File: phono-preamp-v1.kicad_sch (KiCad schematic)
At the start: 0 parts

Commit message: Complete setup of schematic page
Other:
- title: (none) -> Practical MM amplifier #3
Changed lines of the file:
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@@
 	(generator_version "9.0")
 	(paper "A4")
+	(title_block
+		(title "Practical MM amplifier #3")
+		(date "2025-12-29")
+		(rev "0.1")
+		(comment 1 "Small Signal Audio Design, 4th Edition, by Douglas Self")
+		(comment 2 "Based on Signal Transfer design")
+	)
 	(sheet_instances
 		(path "/"

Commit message: Add symbols to schematic
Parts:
- added C1, C18, C2: C_Polarized, symbol Device:C_Polarized
- added C10, C11, C12, C13, C14, C15, C16, C17, C3, C4, C5, C6, C7, C8, C9: C, symbol Device:C
- added J1, J2: Screw_Terminal_01x02, TerminalBlock_4Ucon:TerminalBlock_4Ucon_1x02_P3.50mm_Horizontal, symbol Connector:Screw_Terminal_01x02
- added R1, R10, R11, R12, R13, R14, R15, R2, R3, R4, R5, R6, R7, R8, R9: R, symbol Device:R
- added U1, U2: NE5534, symbol Amplifier_Operational:NE5534

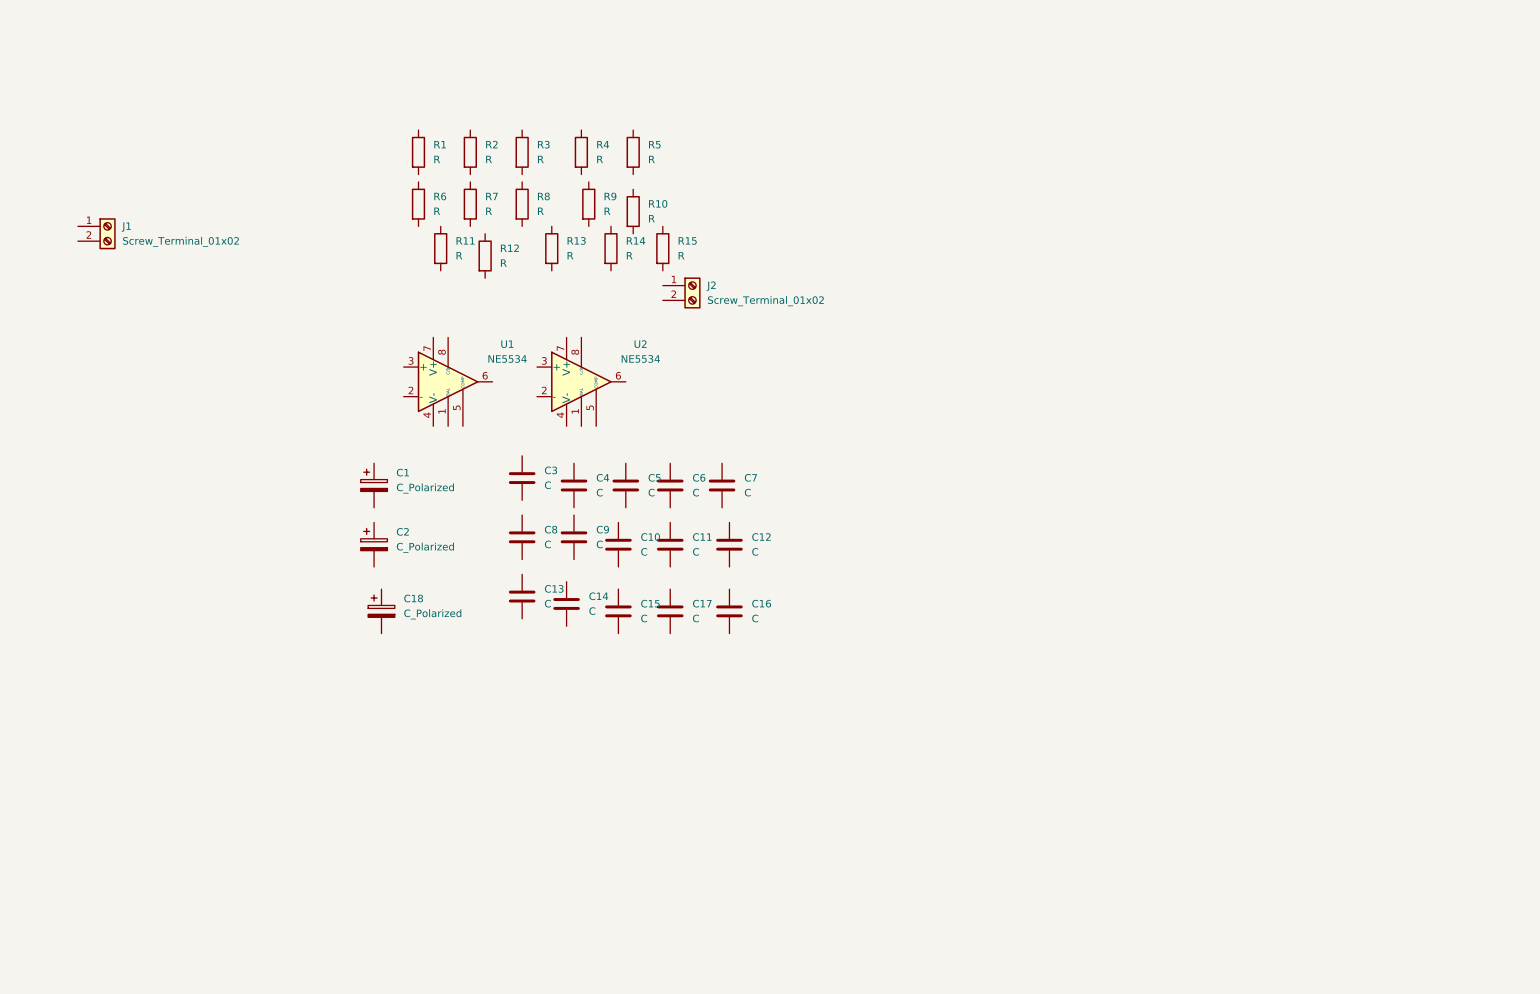
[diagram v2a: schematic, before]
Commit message: Arrange symbols; add footprints
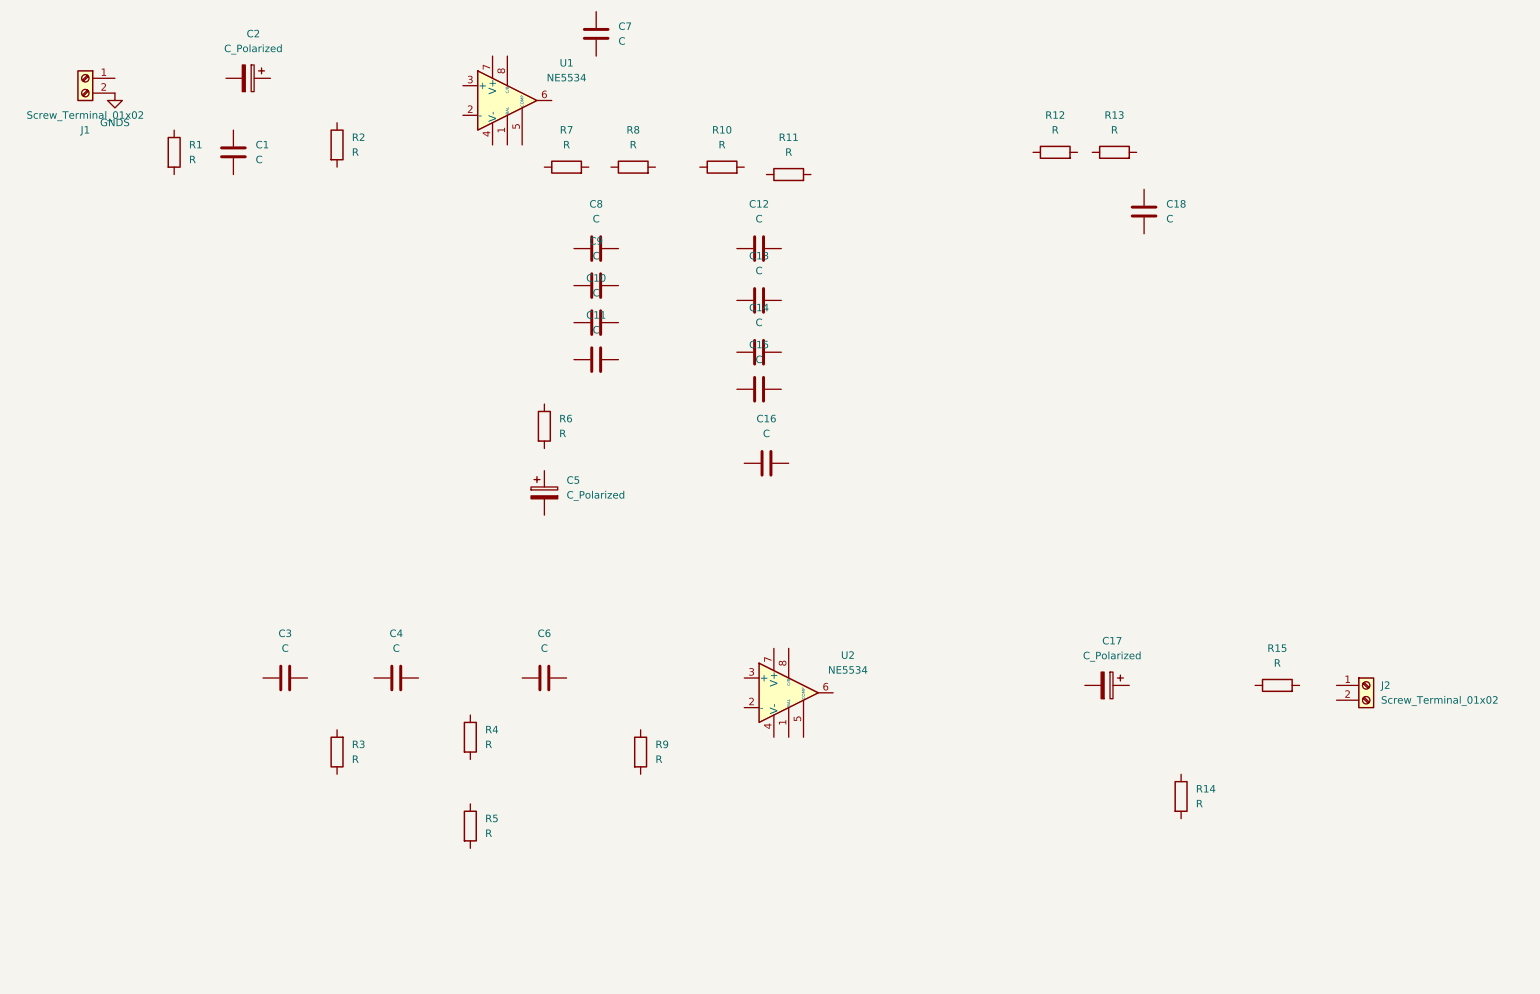
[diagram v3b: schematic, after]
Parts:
- C1: renamed from C3; footprint (none) -> Capacitor_SMD:C_0805_2012Metric_Pad1.18x1.45mm_HandSolder
- C10: renamed from C7; footprint (none) -> Capacitor_SMD:C_0805_2012Metric_Pad1.18x1.45mm_HandSolder
- C11: renamed from C8; footprint (none) -> Capacitor_SMD:C_0805_2012Metric_Pad1.18x1.45mm_HandSolder
- C12: renamed from C13; footprint (none) -> Capacitor_SMD:C_0805_2012Metric_Pad1.18x1.45mm_HandSolder
- C13: renamed from C9; footprint (none) -> Capacitor_SMD:C_0805_2012Metric_Pad1.18x1.45mm_HandSolder
- C14: renamed from C10; footprint (none) -> Capacitor_SMD:C_0805_2012Metric_Pad1.18x1.45mm_HandSolder
- C15: renamed from C11; footprint (none) -> Capacitor_SMD:C_0805_2012Metric_Pad1.18x1.45mm_HandSolder
- C16: renamed from C12; footprint (none) -> Capacitor_SMD:C_0805_2012Metric_Pad1.18x1.45mm_HandSolder
- C17: renamed from C18; footprint (none) -> Capacitor_THT:C_Radial_D4.0mm_H7.0mm_P1.50mm
- C18: renamed from C14; footprint (none) -> Capacitor_SMD:C_0805_2012Metric_Pad1.18x1.45mm_HandSolder
- C2: renamed from C1; footprint (none) -> Capacitor_THT:C_Radial_D6.3mm_H11.0mm_P2.50mm
- C3: renamed from C15; footprint (none) -> Capacitor_SMD:C_0805_2012Metric_Pad1.18x1.45mm_HandSolder
- C4: renamed from C17; footprint (none) -> Capacitor_SMD:C_0805_2012Metric_Pad1.18x1.45mm_HandSolder
- C5: renamed from C2; footprint (none) -> Capacitor_THT:C_Radial_D6.3mm_H11.0mm_P2.50mm
- C6: renamed from C16; footprint (none) -> Capacitor_SMD:C_0805_2012Metric_Pad1.18x1.45mm_HandSolder
- C7: renamed from C4; footprint (none) -> Capacitor_SMD:C_0805_2012Metric_Pad1.18x1.45mm_HandSolder
- C8: renamed from C5; footprint (none) -> Capacitor_SMD:C_0805_2012Metric_Pad1.18x1.45mm_HandSolder
- C9: renamed from C6; footprint (none) -> Capacitor_SMD:C_0805_2012Metric_Pad1.18x1.45mm_HandSolder
- R1, R14, R15, R2: footprint (none) -> Resistor_SMD:R_0805_2012Metric_Pad1.20x1.40mm_HandSolder
- R10: renamed from R6; footprint (none) -> Resistor_SMD:R_0805_2012Metric_Pad1.20x1.40mm_HandSolder
- R11: renamed from R7; footprint (none) -> Resistor_SMD:R_0805_2012Metric_Pad1.20x1.40mm_HandSolder
- R12: renamed from R8; footprint (none) -> Resistor_SMD:R_0805_2012Metric_Pad1.20x1.40mm_HandSolder
- R13: renamed from R9; footprint (none) -> Resistor_SMD:R_0805_2012Metric_Pad1.20x1.40mm_HandSolder
- R3: renamed from R10; footprint (none) -> Resistor_SMD:R_0805_2012Metric_Pad1.20x1.40mm_HandSolder
- R4: renamed from R11; footprint (none) -> Resistor_SMD:R_0805_2012Metric_Pad1.20x1.40mm_HandSolder
- R5: renamed from R12; footprint (none) -> Resistor_SMD:R_0805_2012Metric_Pad1.20x1.40mm_HandSolder
- R6: renamed from R5; footprint (none) -> Resistor_SMD:R_0805_2012Metric_Pad1.20x1.40mm_HandSolder
- R7: renamed from R3; footprint (none) -> Resistor_SMD:R_0805_2012Metric_Pad1.20x1.40mm_HandSolder
- R8: renamed from R4; footprint (none) -> Resistor_SMD:R_0805_2012Metric_Pad1.20x1.40mm_HandSolder
- R9: renamed from R13; footprint (none) -> Resistor_SMD:R_0805_2012Metric_Pad1.20x1.40mm_HandSolder
- U1, U2: footprint (none) -> Package_SO:SOIC-8_3.9x4.9mm_P1.27mm
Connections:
- net GNDS: now reaches J1.2 (Pin_2)
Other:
- moved on the sheet: C1, C10, C11, C12, C13, C14, C15, C16, C17, C18, C2, C3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

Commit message: Add component values
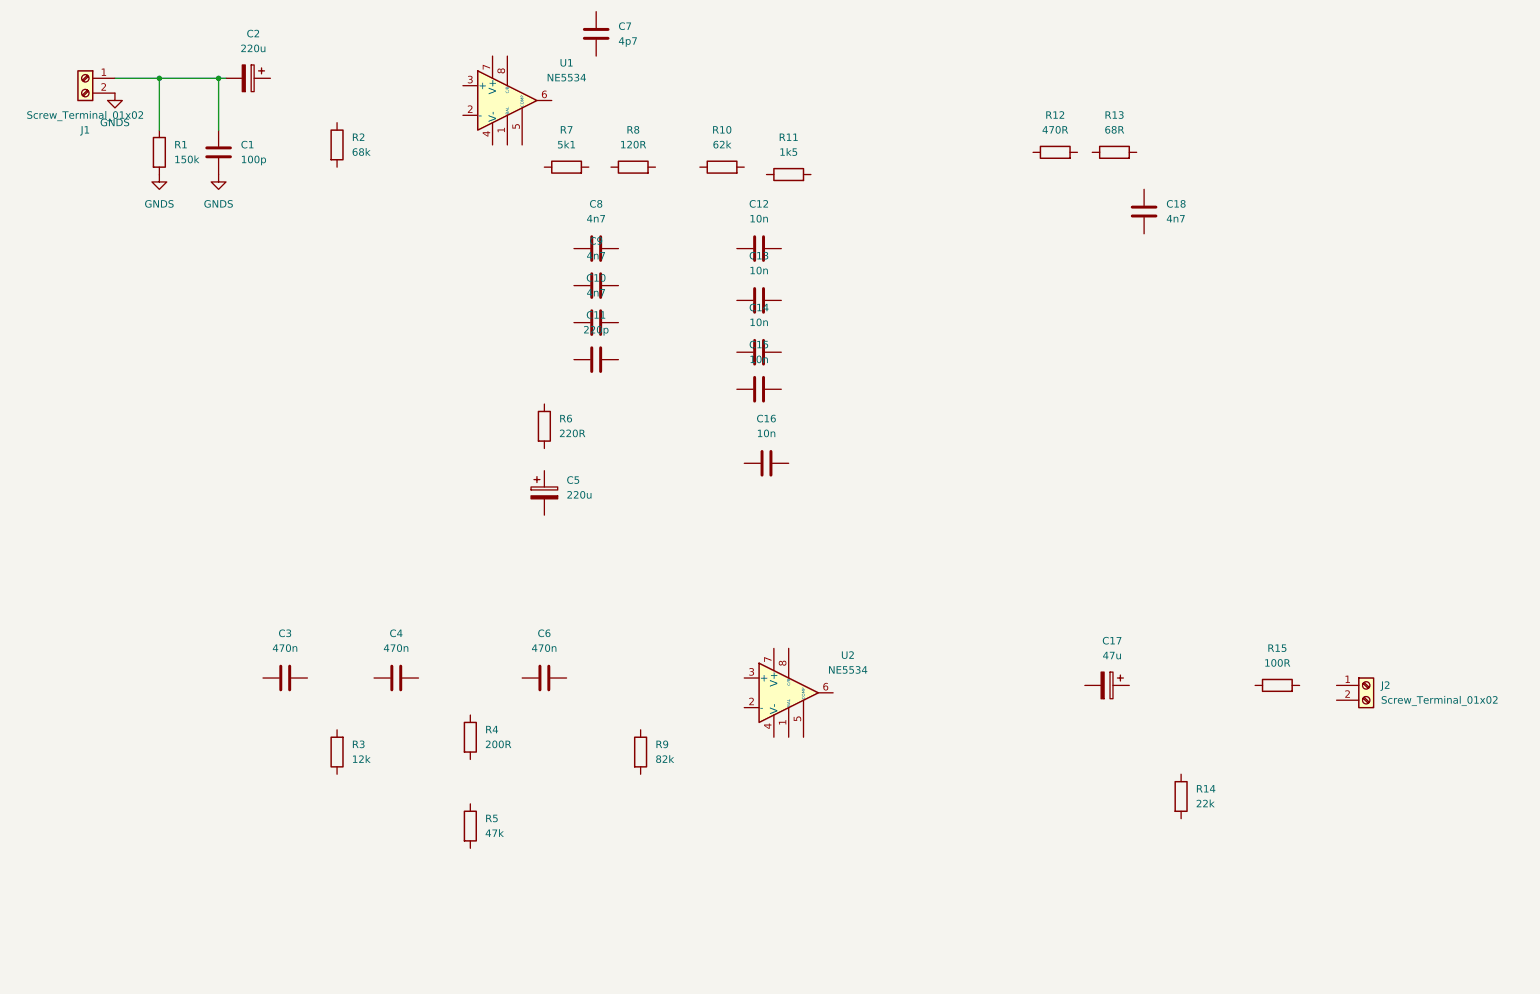
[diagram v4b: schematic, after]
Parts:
- C1: value C -> 100p
- C10, C18, C8, C9: value C -> 4n7
- C11: value C -> 220p
- C12, C13, C14, C15, C16: value C -> 10n
- C17: value C_Polarized -> 47u
- C2, C5: value C_Polarized -> 220u
- C3, C4, C6: value C -> 470n
- C7: value C -> 4p7
- R1: value R -> 150k
- R10: value R -> 62k
- R11: value R -> 1k5
- R12: value R -> 470R
- R13: value R -> 68R
- R14: value R -> 22k
- R15: value R -> 100R
- R2: value R -> 68k
- R3: value R -> 12k
- R4: value R -> 200R
- R5: value R -> 47k
- R6: value R -> 220R
- R7: value R -> 5k1
- R8: value R -> 120R
- R9: value R -> 82k
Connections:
- net GNDS: now also C1.2, R1.2
- net at C2.2: now also C1.1, J1.1 (Pin_1), R1.1
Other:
- moved on the sheet: C1, R1

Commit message: Reannotate symbols; clean up schematic; run simulations
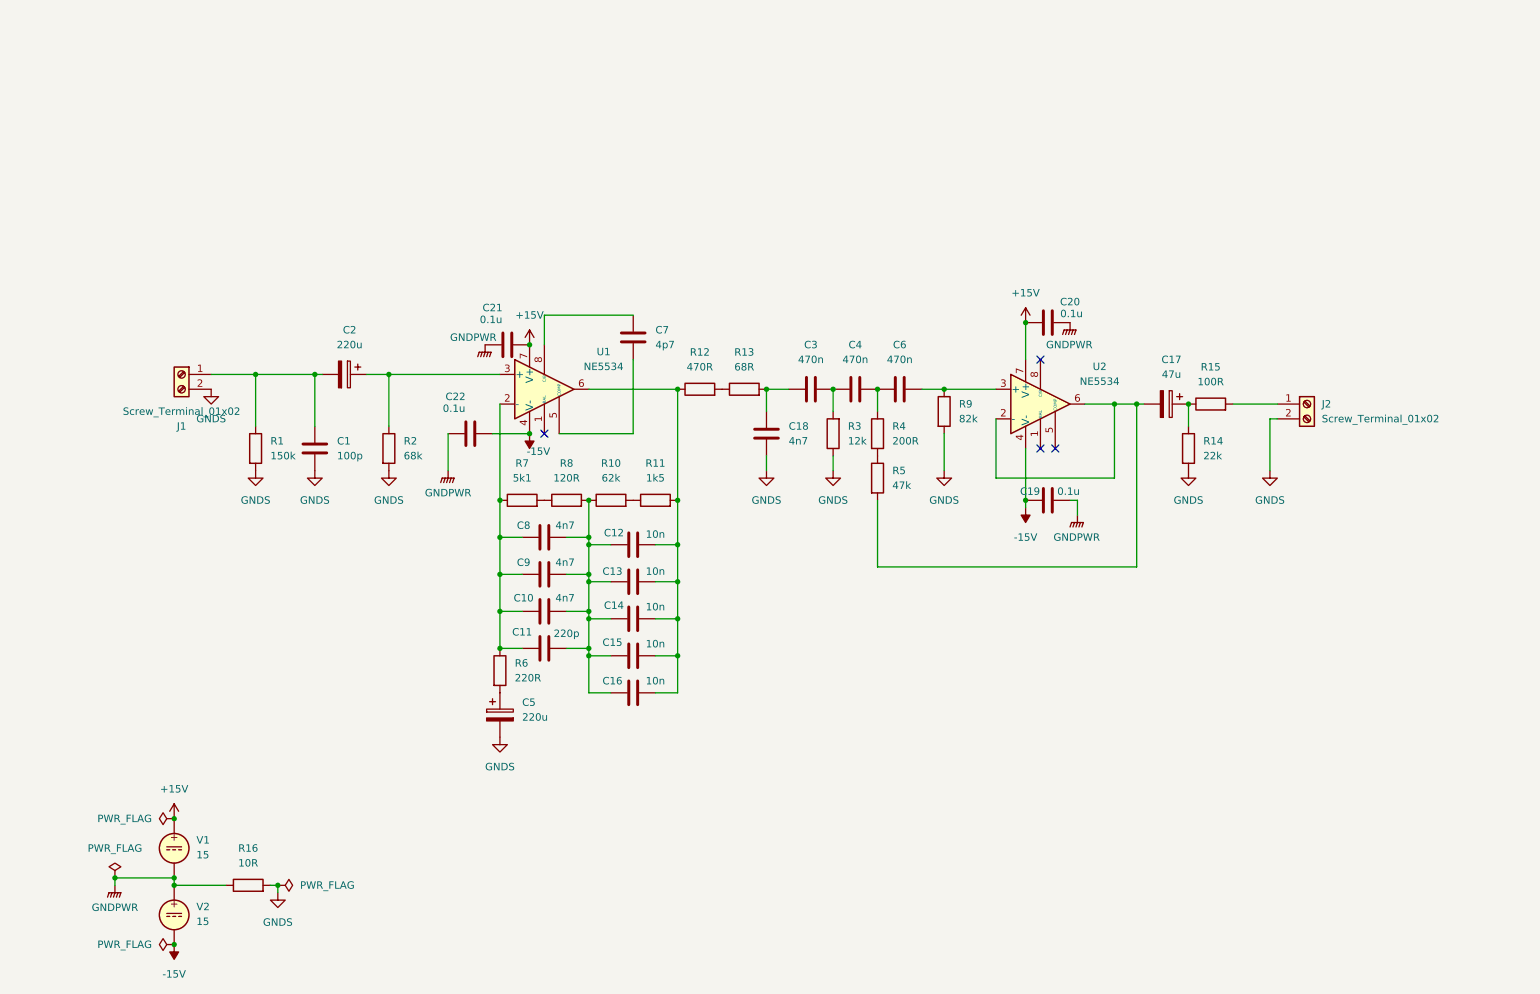
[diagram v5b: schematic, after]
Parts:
- added C19, C20, C21, C22: 0.1u, symbol Device:C
- added R16: 10R, symbol Device:R
- added V1, V2: 15, symbol Simulation_SPICE:VDC
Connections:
- net GNDS: now also C18.1, C5.2, J2.2 (Pin_2), R14.2, R2.2, R3.1, R9.2, R16.2
- net at R13.1: now also R12.2
- net at R13.2: now also C18.2, C3.1
- net at C2.1: now also R2.1, U1.3 (+)
- net at U1.2 (-): now also C10.1, C11.1, C8.1, C9.1, R6.1, R7.1
- net -15V: now reaches U1.4 (V-)
- net -15V: now also U2.4 (V-), C19.1, C22.2, V2.2
- net at U1.5 (COMP): now also C7.2
- net at U1.6: now also C12.2, C13.2, C14.2, C15.2, C16.2, R11.2, R12.1
- net +15V: now reaches U1.7 (V+)
- net +15V: now also U2.7 (V+), C20.1, C21.2, V1.1
- net at U1.8 (C/B): now also C7.1
- net at C6.1: now also C4.2, R4.1
- net at C6.2: now also R9.1, U2.3 (+)
- net at R11.1: now also R10.2
- net at R3.2: now also C3.2, C4.1
- net at R5.1: now also R4.2
- net at R5.2: now also C17.2, U2.2 (-), U2.6
- net at C14.1: now also C10.2, C11.2, C12.1, C13.1, C15.1, C16.1, C8.2, C9.2, R10.1, R8.2
- net at R14.1: now also C17.1, R15.1
- net at C5.1: now also R6.2
- net at R7.2: now also R8.1
- net at J2.1 (Pin_1): now also R15.2
- new net GNDPWR: C19.2, C20.2, C21.1, C22.1, R16.1, V1.2, V2.1
- no-connect marks 0 -> 4
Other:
- moved on the sheet: C1, C10, C11, C12, C13, C14, C15, C16, C17, C18, C2, C3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
